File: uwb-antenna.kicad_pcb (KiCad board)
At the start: 2 copper layers, 30 x 57 mm, 55 parts, among them J1 USB C, J2 Battery, J3 TC2030-NL, SW1 ~{PB}, SW2 BOOT0, SW4 ~{SR}, U1 STM6600, U2 BQ24074RGT, U3 TPS63001, U4 TPD2EUSB30, U5 STM32L432KBUx

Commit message: minors on PCB
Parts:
- moved C13 1.91 mm to (126.0, 104.9), turned to 180 degrees
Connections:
- U5 pad 2: /UWB_RST -> unconnected-(U5-PC14-Pad2)
- U5 pad 3: /WAKEUP -> unconnected-(U5-PC15-Pad3)
- U5 pad 6: unconnected-(U5-PA0-Pad6) -> /WAKEUP
- U5 pad 7: unconnected-(U5-PA1-Pad7) -> /UWB_RST
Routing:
- net /UWB_RST: track 38.8 -> 44.1 mm
- net /WAKEUP: track 40.0 -> 44.0 mm
- net +3.3V: track 90.4 -> 91.9 mm
- net GND: vias 39 -> 48
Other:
- board text added: "+"
- board text added: "-"
- board text added: "Nicolas Farabegoli"
- board text added: "Rev. A - 09/2025"

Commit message: feat: minors in traces and routing
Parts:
- added R18: 20K, Resistor_SMD:R_0402_1005Metric, F.Cu at (143.2, 114.4)
- added R3: 10K, Resistor_SMD:R_0402_1005Metric, F.Cu at (143.2, 113.3)
- moved C2 0.61 mm to (129.2, 101.2), turned to -90 degrees
- moved R1 0.05 mm to (140.7, 119.7)
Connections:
- U5 pad 9: unconnected-(U5-PA3-Pad9) -> /BATT_READ
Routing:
- net /BATT_READ: track 0.00 -> 21.2 mm, vias 0 -> 2
- net /BAT: track 10.8 -> 15.1 mm
- net /SWCLK: track 20.2 -> 20.7 mm
- net GND: vias 48 -> 50
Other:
- board text added: "N. Farabegoli"
- board text added: "Rev. A"
- board text removed: "Nicolas Farabegoli"
- board text removed: "Rev. A - 09/2025"

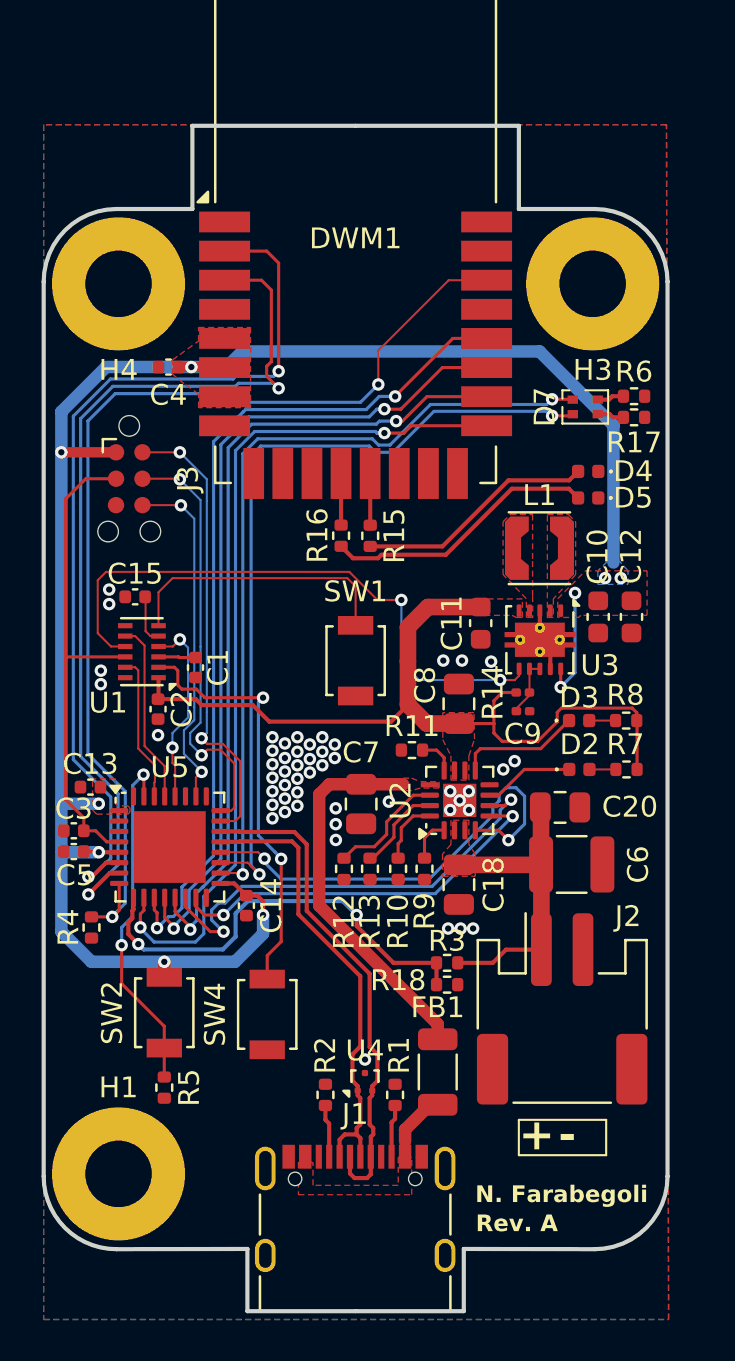
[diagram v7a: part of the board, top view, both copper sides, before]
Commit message: feat: add panelized version
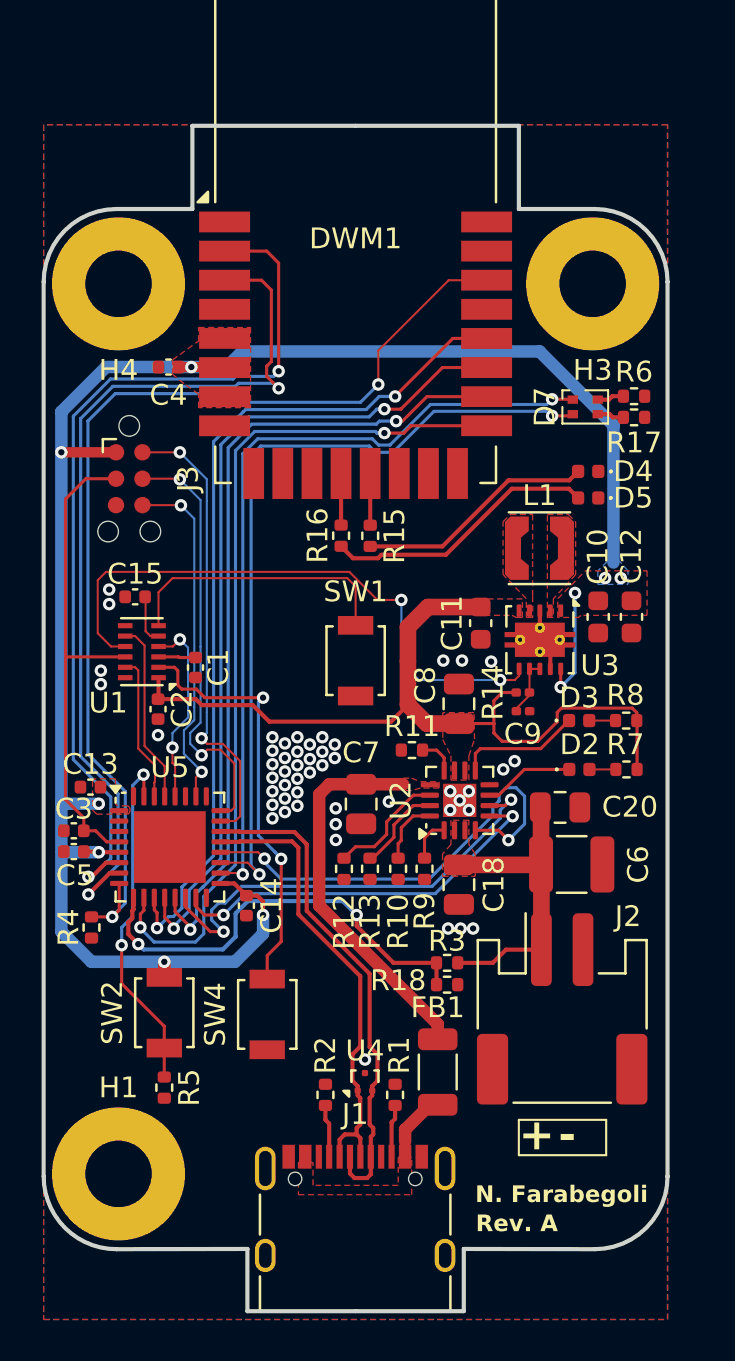
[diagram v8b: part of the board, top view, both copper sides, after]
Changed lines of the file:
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@@
 		(polygon
 			(pts
-				(xy 123.75 130.5) (xy 153.8 130.5) (xy 153.7 73.05) (xy 123.75 73.05)
+				(xy 123.75 130.5) (xy 153.75 130.5) (xy 153.75 73.05) (xy 123.75 73.05)
 			)
 		)
@@
 		(polygon
 			(pts
-				(xy 153.7 73.05) (xy 123.75 73.05) (xy 123.75 130.5) (xy 153.8 130.5)
+				(xy 153.75 73.05) (xy 123.75 73.05) (xy 123.75 130.5) (xy 153.75 130.5)
 			)
 		)
